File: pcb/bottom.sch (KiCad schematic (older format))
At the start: 33 parts, among them J1 1-MALE, J10 TC2030_NL, J2 1-FEMALE, J3 2-MALE, J4 2-FEMALE, J5 3-MALE, J6 3-FEMALE, J7 4-MALE, J8 4-FEMALE, J9 DTR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

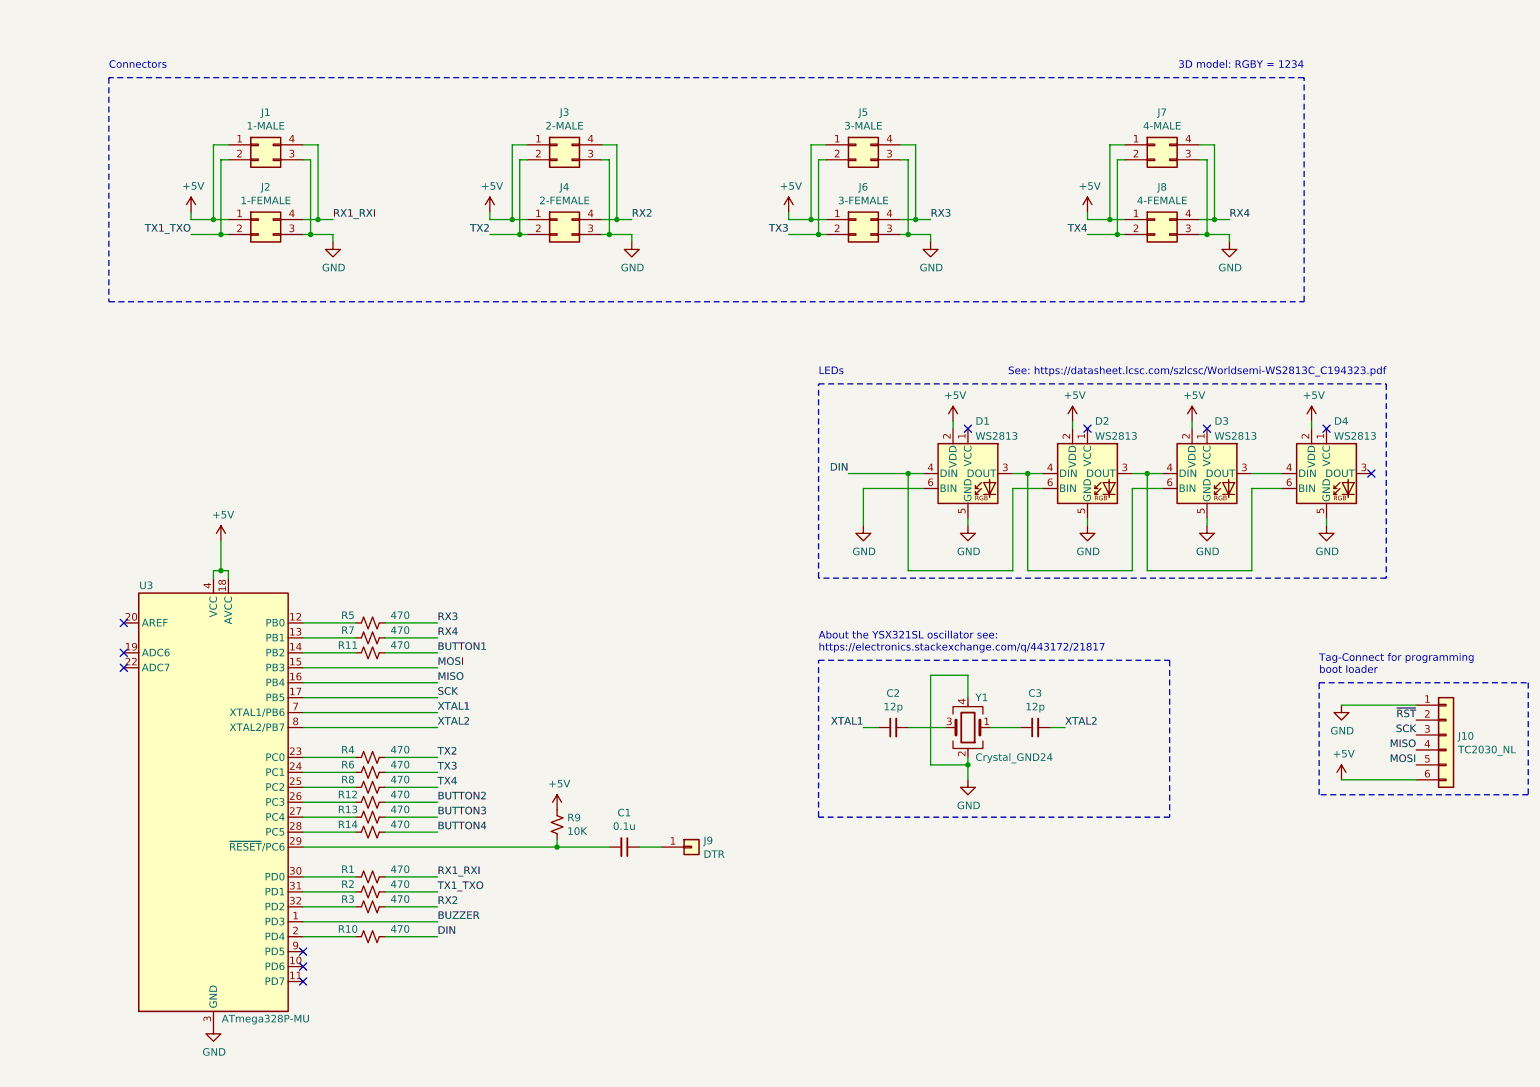
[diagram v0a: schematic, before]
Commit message: Assign footprints and complete BOM
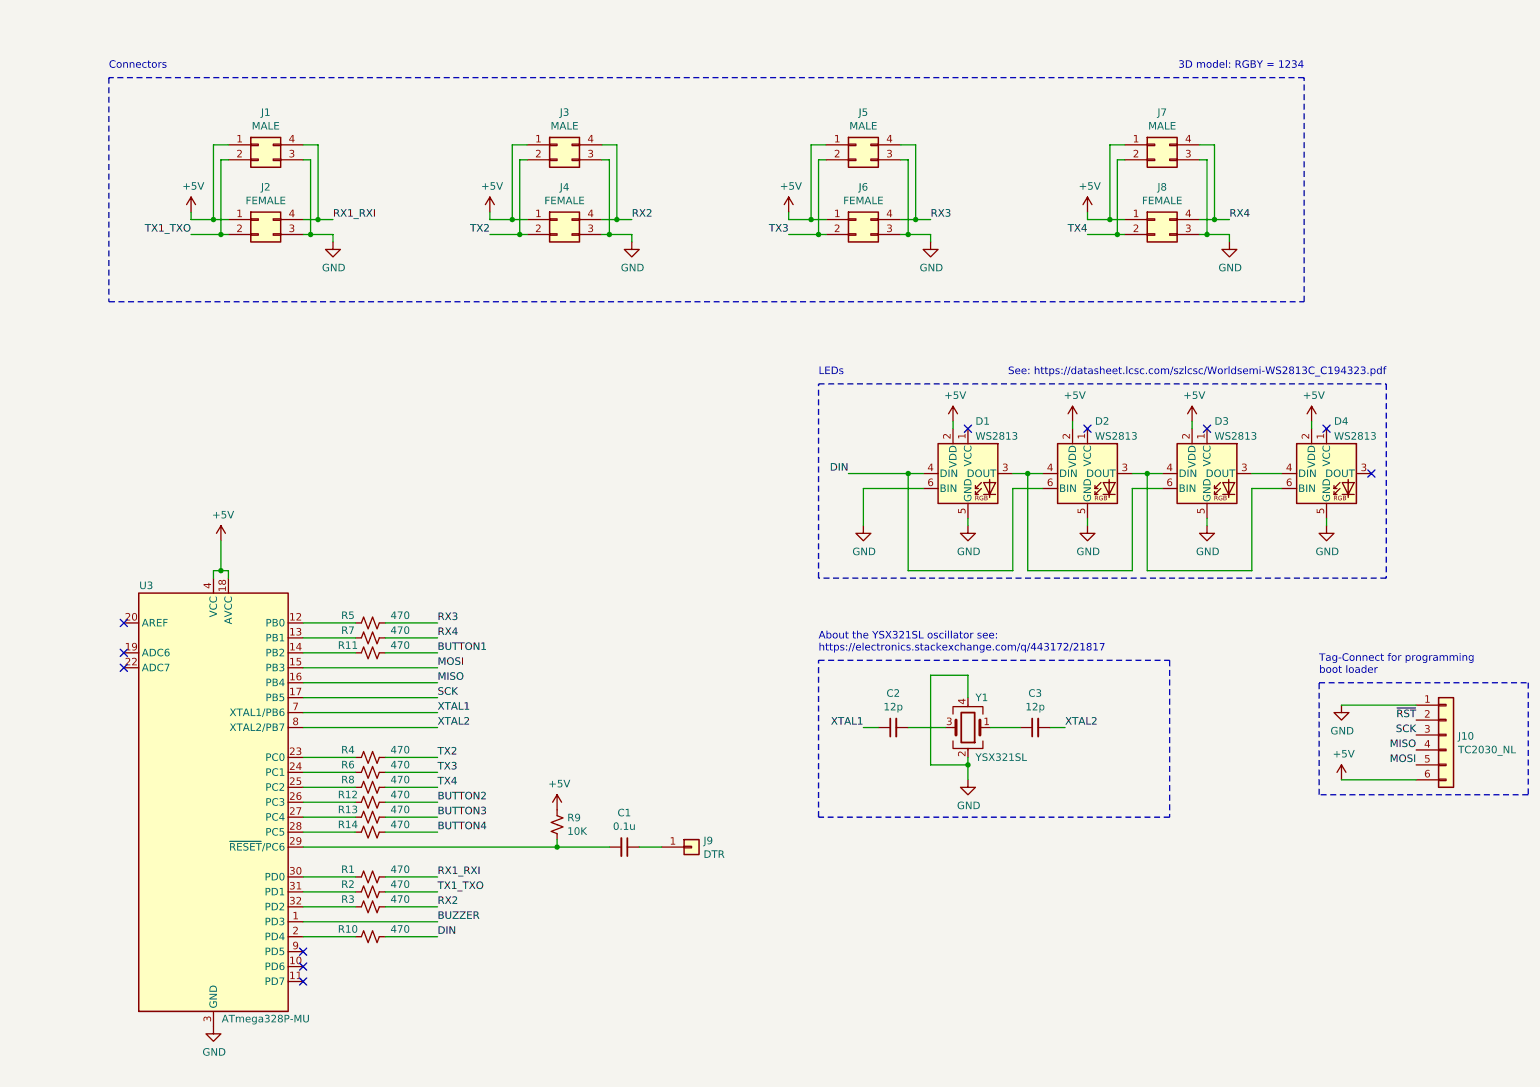
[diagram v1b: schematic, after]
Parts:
- C1: footprint (none) -> Capacitor_SMD:C_0402_1005Metric; LCSC Part # (none) -> C60474; MPN (none) -> CC0402KRX7R7BB104; Manufacturer (none) -> YAGEO; Package (none) -> 0402
- C2, C3: footprint (none) -> Capacitor_SMD:C_0402_1005Metric; LCSC Part # (none) -> C277478; MPN (none) -> CC0201JRNPO9BN120; Manufacturer (none) -> YAGEO; Package (none) -> 0402
- D1, D2, D3, D4: footprint LED_SMD:LED_WS2812_PLCC6_5.0x5.0mm_P1.6mm -> node:WS2813-Mini; LCSC Part # (none) -> C189639; MPN (none) -> WS2813-Mini(WS2813-3535); Manufacturer (none) -> Worldsemi
- J1: value 1-MALE -> MALE; LCSC Part # (none) -> C239333; MPN (none) -> A2541WR-2x2P; Manufacturer (none) -> CJT(Changjiang Connectors)
- J2: value 1-FEMALE -> FEMALE; LCSC Part # (none) -> C239353; MPN (none) -> A2541HWR-2x2P; Manufacturer (none) -> CJT(Changjiang Connectors)
- J3: value 2-MALE -> MALE; LCSC Part # (none) -> C239333; MPN (none) -> A2541WR-2x2P; Manufacturer (none) -> CJT(Changjiang Connectors)
- J4: value 2-FEMALE -> FEMALE; LCSC Part # (none) -> C239353; MPN (none) -> A2541HWR-2x2P; Manufacturer (none) -> CJT(Changjiang Connectors)
- J5: value 3-MALE -> MALE; LCSC Part # (none) -> C239333; MPN (none) -> A2541WR-2x2P; Manufacturer (none) -> CJT(Changjiang Connectors)
- J6: value 3-FEMALE -> FEMALE; LCSC Part # (none) -> C239353; MPN (none) -> A2541HWR-2x2P; Manufacturer (none) -> CJT(Changjiang Connectors)
- J7: value 4-MALE -> MALE; LCSC Part # (none) -> C239333; MPN (none) -> A2541WR-2x2P; Manufacturer (none) -> CJT(Changjiang Connectors)
- J8: value 4-FEMALE -> FEMALE; LCSC Part # (none) -> C239353; MPN (none) -> A2541HWR-2x2P; Manufacturer (none) -> CJT(Changjiang Connectors)
- R1, R10, R11, R12, R13, R14, R2, R3, R4, R5, R6, R7, R8: LCSC Part # (none) -> C106878; Manufacturer (none) -> RALEC; Package (none) -> 0402
- R9: LCSC Part # (none) -> C102629; Manufacturer (none) -> RALEC; Package (none) -> 0402
- U3: LCSC Part # (none) -> C783592; Manufacturer (none) -> Microchip Tech; Package (none) -> VFQFN-32
- Y1: value Crystal_GND24 -> YSX321SL; footprint (none) -> node:YSX321SL; LCSC Part # (none) -> C12668; MPN (none) -> X322516MOB4SI; Manufacturer (none) -> Yangxing Tech

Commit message: Add buzzer and clean up
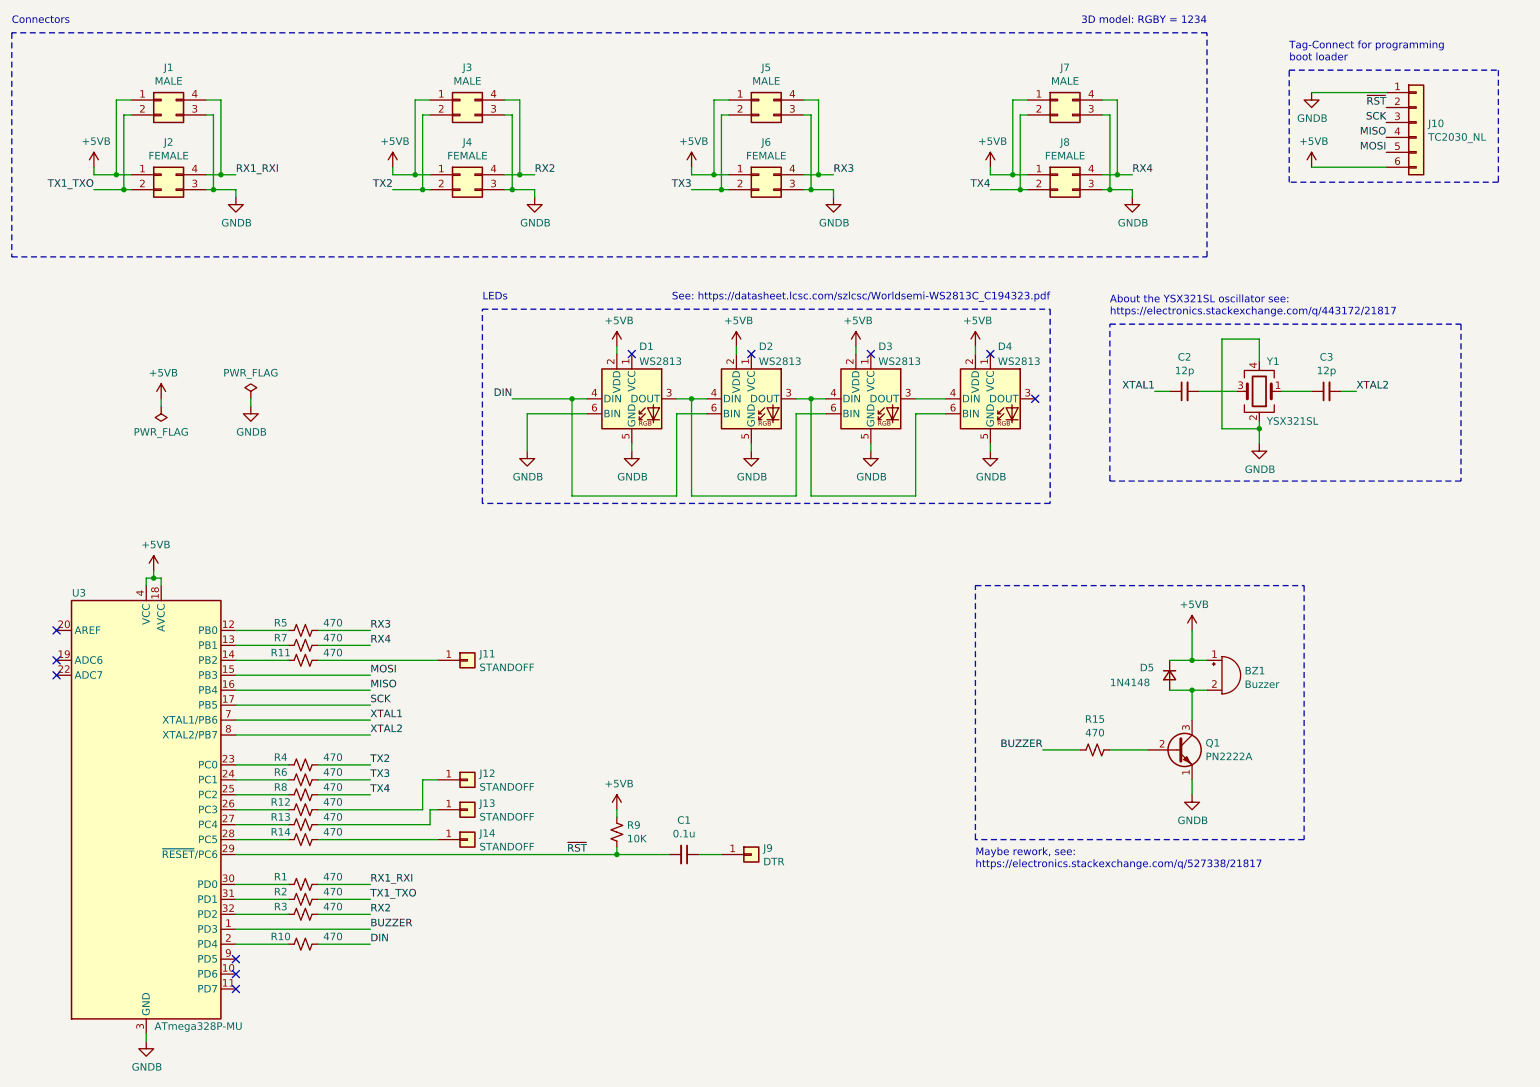
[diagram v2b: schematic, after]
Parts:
- added BZ1: Buzzer, symbol Device:Buzzer
- added D5: 1N4148, symbol Device:D_Small
- added J11, J12, J13, J14: STANDOFF, MountingHole:MountingHole_2.2mm_M2_Pad_Via, symbol Connector_Generic:Conn_01x01
- added Q1: PN2222A, Package_TO_SOT_THT:TO-92_Inline, symbol Transistor_BJT:PN2222A
- added R15: 470, Resistor_SMD:R_0402_1005Metric, symbol Device:R_Small_US
- J9: footprint Connector_Pin:Pin_D1.0mm_L10.0mm -> Connector_PinHeader_2.54mm:PinHeader_1x01_P2.54mm_Vertical
- R1, R10, R11, R12, R13, R14, R2, R3, R4, R5, R6, R7, R8: Min Quantity 100 -> (none); OPL Shenzhen -> (none); SKU 0402WGF4700TCE -> (none)
- R9: Min Quantity 100 -> (none); OPL Shenzhen -> (none); SKU RC0402JR-0710KL -> (none)
- U3: Min Quantity 310010005 -> (none); OPL Seeed -> (none)
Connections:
- net BUZZER: now also R15.2
- net ~RST: now also C1.2, R9.2, U3.29 (~RESET~/PC6)
- net +5V renamed +5VB
- net +5VB: now also BZ1.1 (-), D5.1 (K)
- net BUTTON1: no longer names the net of R11.1
- net BUTTON1: now also J11.1 (Pin_1)
- net BUTTON2: no longer names the net of R12.1
- net BUTTON2: now also J12.1 (Pin_1)
- net BUTTON3: no longer names the net of R13.1
- net BUTTON3: now also J13.1 (Pin_1)
- net BUTTON4: no longer names the net of R14.1
- net BUTTON4: now also J14.1 (Pin_1)
- net GND renamed GNDB
- net GNDB: now also Q1.1 (E)
- new net: BZ1.2 (+), D5.2 (A), Q1.3 (C)
- new net: Q1.2 (B), R15.1
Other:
- note added: "Maybe rework, see:\nhttps://electronics.stackexchange.com/q/527338/21817"
- moved on the sheet: C1, C2, C3, D1, D2, D3, D4, J1, J10, J2, J3, J4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

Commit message: Iterate
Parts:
- added R16: 47, Resistor_SMD:R_0402_1005Metric, symbol Device:R_Small_US
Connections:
- net +5VB: now also R16.2; no longer BZ1.1 (-), D5.1 (K)
- new net: BZ1.1 (-), D5.1 (K), R16.1
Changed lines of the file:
@@
 $Descr A4 11693 8268
 encoding utf-8
-Sheet 3 3
+Sheet 2 3
 Title "Bottom"
 Date ""
@@
 L node:+5VB #PWR01
 U 1 1 5F965E09
-P 8500 4700
-F 0 "#PWR01" H 8500 4550 50  0001 C CNN
-F 1 "+5VB" H 8515 4873 50  0000 C CNN
-F 2 "" H 8500 4700 50  0001 C CNN
-F 3 "" H 8500 4700 50  0001 C CNN
-	1    8500 4700
+P 8500 4400
+F 0 "#PWR01" H 8500 4250 50  0001 C CNN
+F 1 "+5VB" H 8515 4573 50  0000 C CNN
+F 2 "" H 8500 4400 50  0001 C CNN
+F 3 "" H 8500 4400 50  0001 C CNN
+	1    8500 4400
 	1    0    0    -1
 $EndComp
@@
 	8350 4900 8500 4900
 Wire Wire Line
-	8500 4700 8500 4900
+	8500 4750 8500 4900
 Connection ~ 8500 4900
 Wire Wire Line
 	8500 4900 8600 4900
 Wire Notes Line
-	7050 4400 9250 4400
-Wire Notes Line
-	9250 4400 9250 6100
+	7050 4100 9250 4100
+Wire Notes Line
+	9250 4100 9250 6100
 Wire Notes Line
 	9250 6100 7050 6100
 Wire Notes Line
-	7050 6100 7050 4400
+	7050 6100 7050 4100
 Text Notes 7050 6300 0    50   ~ 0
 Maybe rework, see:\nhttps://electronics.stackexchange.com/q/527338/21817
@@
 Wire Wire Line
 	2650 4900 3450 4900
+$Comp
+L Device:R_Small_US R16
+U 1 1 5F8D7356
+P 8500 4650
+F 0 "R16" V 8295 4650 50  0000 C CNN
+F 1 "47" V 8386 4650 50  0000 C CNN
+F 2 "Resistor_SMD:R_0402_1005Metric" H 8500 4650 50  0001 C CNN
+F 3 "~" H 8500 4650 50  0001 C CNN
+	1    8500 4650
+	-1   0    0    1
+$EndComp
+Wire Wire Line
+	8500 4550 8500 4400
 $EndSCHEMATC

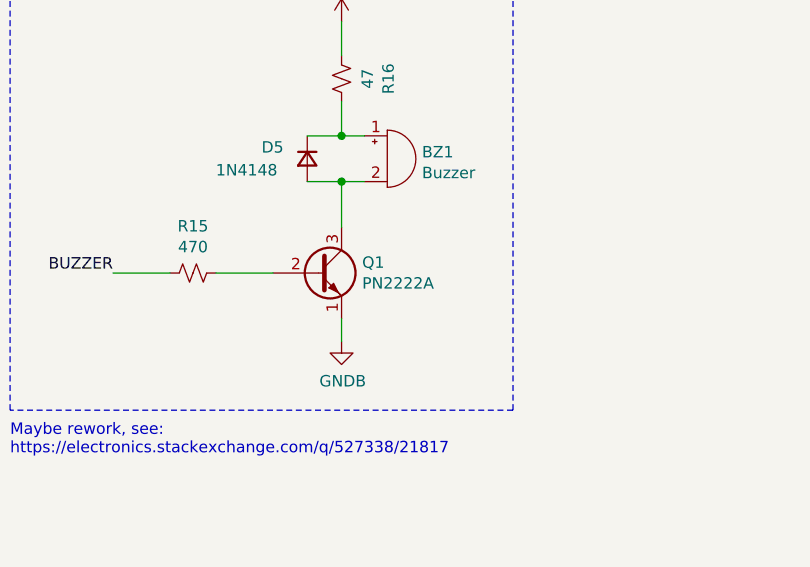
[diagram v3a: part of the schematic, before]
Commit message: Select transistor for buzzer
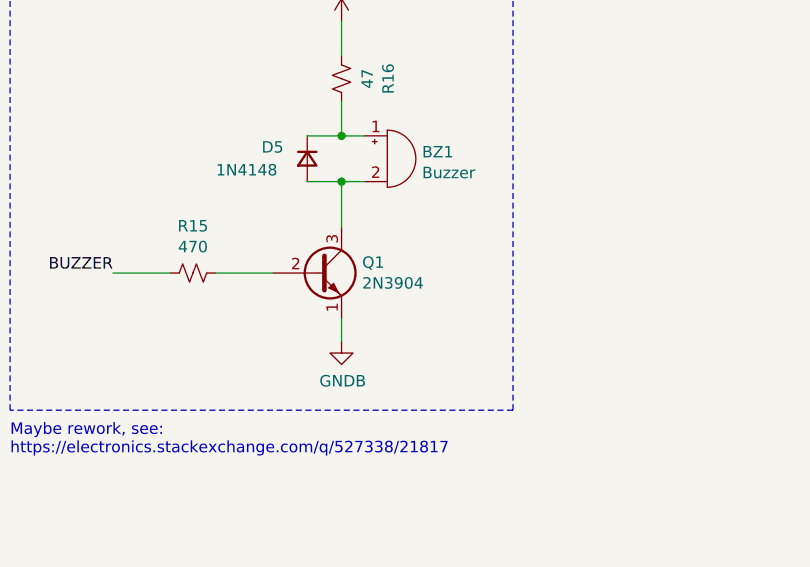
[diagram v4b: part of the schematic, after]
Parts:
- D5: LCSC Part # (none) -> C8667; MPN (none) -> PMBT3904,215; Manufacturer (none) -> Nexperia
- Q1: value PN2222A -> 2N3904; footprint Package_TO_SOT_THT:TO-92_Inline -> digikey-footprints:SOT23-6L
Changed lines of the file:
@@
 F 1 "1N4148" V 8400 4600 50  0000 L CNN
 F 2 "" V 8350 5000 50  0001 C CNN
-F 3 "~" V 8350 5000 50  0001 C CNN
+F 3 "https://datasheet.lcsc.com/szlcsc/1811141222_Nexperia-PMBT3904-215_C8667.pdf" V 8350 5000 50  0001 C CNN
+F 4 "C8667" H 8350 5000 50  0001 C CNN "LCSC Part #"
+F 5 "PMBT3904,215" H 8350 5000 50  0001 C CNN "MPN"
+F 6 "Nexperia" H 8350 5000 50  0001 C CNN "Manufacturer"
 	1    8350 5000
 	0    1    1    0
@@
 P 8400 5500
 F 0 "Q1" H 8590 5546 50  0000 L CNN
-F 1 "PN2222A" H 8590 5455 50  0000 L CNN
-F 2 "Package_TO_SOT_THT:TO-92_Inline" H 8600 5425 50  0001 L CIN
+F 1 "2N3904" H 8590 5455 50  0000 L CNN
+F 2 "digikey-footprints:SOT23-6L" H 8600 5425 50  0001 L CIN
 F 3 "https://www.onsemi.com/pub/Collateral/PN2222-D.PDF" H 8400 5500 50  0001 L CNN
 	1    8400 5500

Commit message: Fix: Wrong footprint for transistor
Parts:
- Q1: footprint digikey-footprints:SOT23-6L -> Package_TO_SOT_SMD:SOT-23
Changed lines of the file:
@@
 F 0 "Q1" H 8590 5546 50  0000 L CNN
 F 1 "2N3904" H 8590 5455 50  0000 L CNN
-F 2 "digikey-footprints:SOT23-6L" H 8600 5425 50  0001 L CIN
+F 2 "Package_TO_SOT_SMD:SOT-23" H 8600 5425 50  0001 L CIN
 F 3 "https://www.onsemi.com/pub/Collateral/PN2222-D.PDF" H 8400 5500 50  0001 L CNN
 	1    8400 5500

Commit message: Fix: Missing and conflicting values in symbol table
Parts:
- Q1: LCSC Part # (none) -> C8667; MPN (none) -> PMBT3904,215; Manufacturer (none) -> Nexperia; Package (none) -> SOT-23
- R1, R10, R11, R12, R13, R14, R2, R3, R4, R5, R6, R7, R8: LCSC Part # C106878 -> C114949; MPN 0402WGF4700TCE -> RC0402JR-07470RL; Manufacturer RALEC -> YAGEO
- R15: LCSC Part # (none) -> C114949; MPN (none) -> RC0402JR-07470RL; Manufacturer (none) -> YAGEO; Package (none) -> 0402
- R16: LCSC Part # (none) -> C137973; MPN (none) -> RC0402FR-0747RL; Manufacturer (none) -> YAGEO; Package (none) -> 0402

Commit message: Add footprint for diode
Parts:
- D5: LCSC Part # C8667 -> C60580; MPN PMBT3904,215 -> 1N4148WS-7-F; Manufacturer Nexperia -> Diodes Incorporated; Package (none) -> SOD-323
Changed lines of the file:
@@
 F 1 "1N4148" V 8400 4600 50  0000 L CNN
 F 2 "" V 8350 5000 50  0001 C CNN
-F 3 "https://datasheet.lcsc.com/szlcsc/1811141222_Nexperia-PMBT3904-215_C8667.pdf" V 8350 5000 50  0001 C CNN
-F 4 "C8667" H 8350 5000 50  0001 C CNN "LCSC Part #"
-F 5 "PMBT3904,215" H 8350 5000 50  0001 C CNN "MPN"
-F 6 "Nexperia" H 8350 5000 50  0001 C CNN "Manufacturer"
+F 3 "https://datasheet.lcsc.com/szlcsc/1810251613_Diodes-Incorporated-1N4148WS-7-F_C60580.pdf" V 8350 5000 50  0001 C CNN
+F 4 "C60580" H 8350 5000 50  0001 C CNN "LCSC Part #"
+F 5 "1N4148WS-7-F" H 8350 5000 50  0001 C CNN "MPN"
+F 6 "Diodes Incorporated" H 8350 5000 50  0001 C CNN "Manufacturer"
+F 7 "SOD-323" H 8350 5000 50  0001 C CNN "Package"
 	1    8350 5000
 	0    1    1    0

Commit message: Assign footprints
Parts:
- BZ1: footprint (none) -> node:MLT-5020; LCSC Part # (none) -> C94598; MPN (none) -> MLT-5020; Manufacturer (none) -> Jiangsu Huaneng Elec
- D5: footprint (none) -> Diode_SMD:D_SOD-323
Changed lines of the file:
@@
 F 0 "BZ1" H 8852 5029 50  0000 L CNN
 F 1 "Buzzer" H 8852 4938 50  0000 L CNN
-F 2 "" V 8675 5100 50  0001 C CNN
-F 3 "~" V 8675 5100 50  0001 C CNN
+F 2 "node:MLT-5020" V 8675 5100 50  0001 C CNN
+F 3 "https://datasheet.lcsc.com/szlcsc/1811151523_Jiangsu-Huaneng-Elec-MLT-5020_C94598.pdf" V 8675 5100 50  0001 C CNN
+F 4 "C94598" H 8700 5000 50  0001 C CNN "LCSC Part #"
+F 5 "MLT-5020" H 8700 5000 50  0001 C CNN "MPN"
+F 6 "Jiangsu Huaneng Elec" H 8700 5000 50  0001 C CNN "Manufacturer"
 	1    8700 5000
 	1    0    0    -1
@@
 F 0 "D5" V 8300 4800 50  0000 L CNN
 F 1 "1N4148" V 8400 4600 50  0000 L CNN
-F 2 "" V 8350 5000 50  0001 C CNN
+F 2 "Diode_SMD:D_SOD-323" V 8350 5000 50  0001 C CNN
 F 3 "https://datasheet.lcsc.com/szlcsc/1810251613_Diodes-Incorporated-1N4148WS-7-F_C60580.pdf" V 8350 5000 50  0001 C CNN
 F 4 "C60580" H 8350 5000 50  0001 C CNN "LCSC Part #"
